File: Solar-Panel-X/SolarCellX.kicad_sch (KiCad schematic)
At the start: 55 parts, among them J1 XF2M-1015-1A, U2 Value, U3 TSL2561

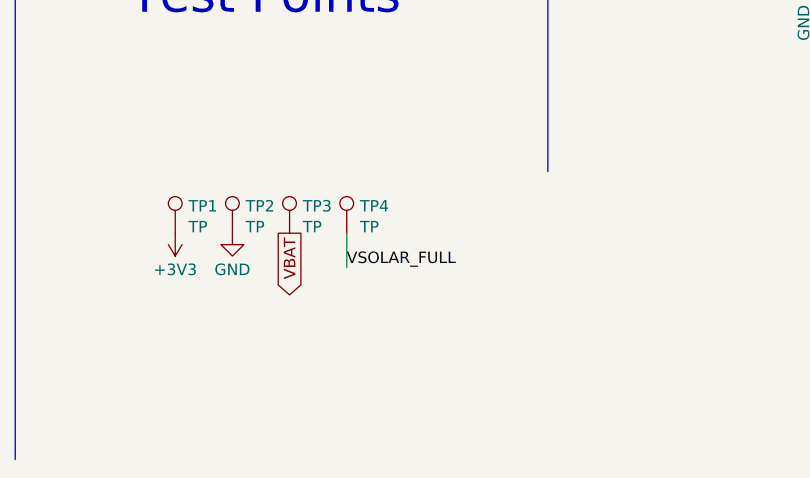
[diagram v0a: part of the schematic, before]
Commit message: Moved board connectors to North board edges
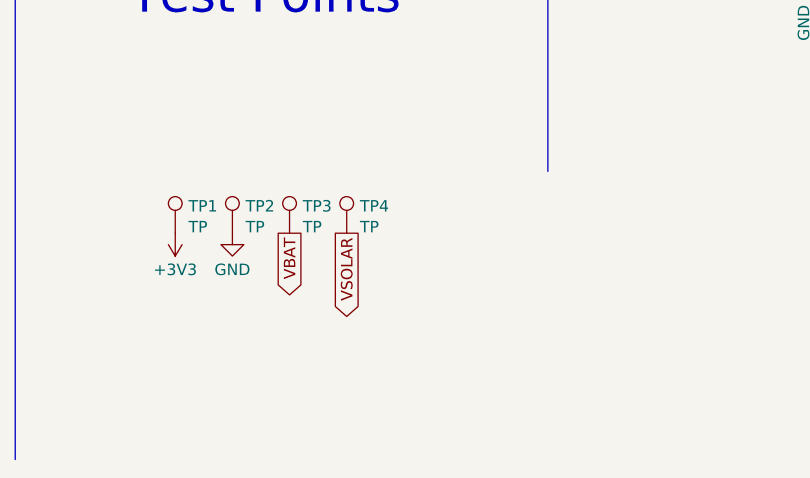
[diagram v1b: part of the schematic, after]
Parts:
- C6: footprint Capacitor_SMD:C_0603_1608Metric -> Capacitor_SMD:C_0402_1005Metric
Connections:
- net VSOLAR: now also TP4.1
- net VSOLAR_FULL: no longer TP4.1
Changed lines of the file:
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@@
-    (stroke (width 0) (type default) (color 0 0 0 0))
-  )
-  (wire (pts (xy 213.36 178.816) (xy 213.36 182.626))
     (stroke (width 0) (type default) (color 0 0 0 0))
   )
@@
   (label "GND" (at 197.104 75.946 0)
     (effects (font (size 0.254 0.254)) (justify left bottom))
-  )
-  (label "VSOLAR_FULL" (at 213.36 182.626 0)
-    (effects (font (size 1.27 1.27)) (justify left bottom))
   )
   (label "VBAT" (at 146.304 75.946 270)
@@
     (property "Intersheet References" "${INTERSHEET_REFS}" (id 0) (at 26.67 21.336 0)
       (effects (font (size 1.27 1.27)) hide)
+    )
+  )
+  (global_label "VSOLAR" (shape output) (at 213.36 178.816 270) (fields_autoplaced)
+    (effects (font (size 1.27 1.27)) (justify right))
+    (property "Intersheet References" "${INTERSHEET_REFS}" (id 0) (at 213.2806 188.1554 90)
+      (effects (font (size 1.27 1.27)) (justify right) hide)
     )
   )
@@
       (effects (font (size 1.2 1.2)) (justify left))
     )
-    (property "Footprint" "Capacitor_SMD:C_0603_1608Metric" (id 2) (at 147.2692 88.646 0)
+    (property "Footprint" "Capacitor_SMD:C_0402_1005Metric" (id 2) (at 147.2692 88.646 0)
       (effects (font (size 1.27 1.27)) hide)
     )
@@
     )
     (path "/00000000-0000-0000-0000-000088e586df"
-      (reference "C6") (unit 1) (value "100uF") (footprint "Capacitor_SMD:C_0603_1608Metric")
+      (reference "C6") (unit 1) (value "100uF") (footprint "Capacitor_SMD:C_0402_1005Metric")
     )
     (path "/00000000-0000-0000-0000-00009549b0a9"

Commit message: Made Requested Changes
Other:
- note added: "Solar Panel Board X"
- company: (none) -> REx Lab Carnegie Mellon University
- title: Solar Panel Board X -> PyCubed Mini
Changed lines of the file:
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@@
   (paper "USLegal")
   (title_block
-    (title "Solar Panel Board X")
-    (date "2022-02-23")
+    (title "PyCubed Mini")
+    (date "2022-03-04")
     (rev "3")
+    (company "REx Lab Carnegie Mellon University")
+    (comment 1 "Z.Manchester")
+    (comment 2 "N.Khera")
+    (comment 3 "M.Holliday")
   )
   (junction (at 38.608 50.546) (diameter 0) (color 0 0 0 0)
@@
     (effects (font (size 4 4)) (justify left bottom))
   )
+  (text "Solar Panel Board X" (at 262.382 182.118 0)
+    (effects (font (size 3.81 3.81) (thickness 0.762) bold) (justify left bottom))
+  )
   (text "VOUT=1.21V*((ROUT2+ROUT1)/ROUT1)" (at 93.218 134.366 0)
